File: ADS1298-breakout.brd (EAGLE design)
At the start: 33 parts, among them IC2 TPS73250DBVT, IC3 TPS73233DBVT

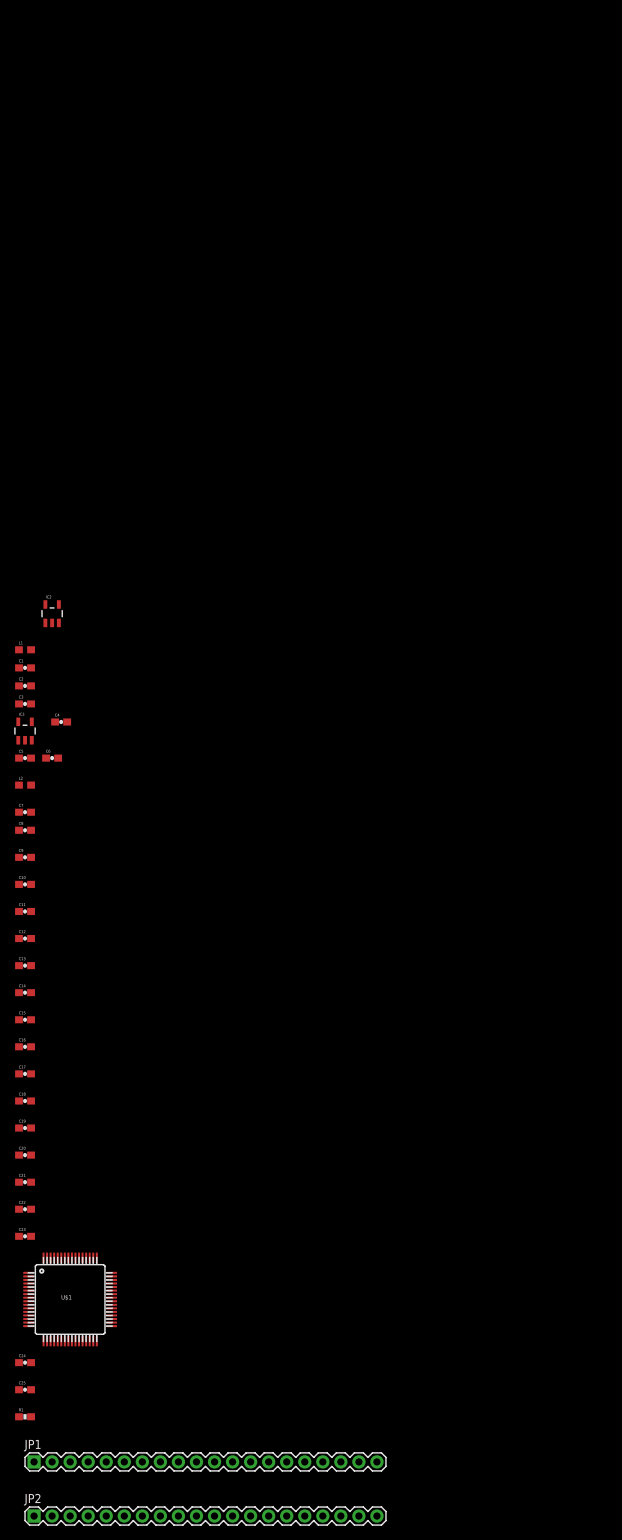
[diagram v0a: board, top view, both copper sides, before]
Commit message: schematic passes ERC
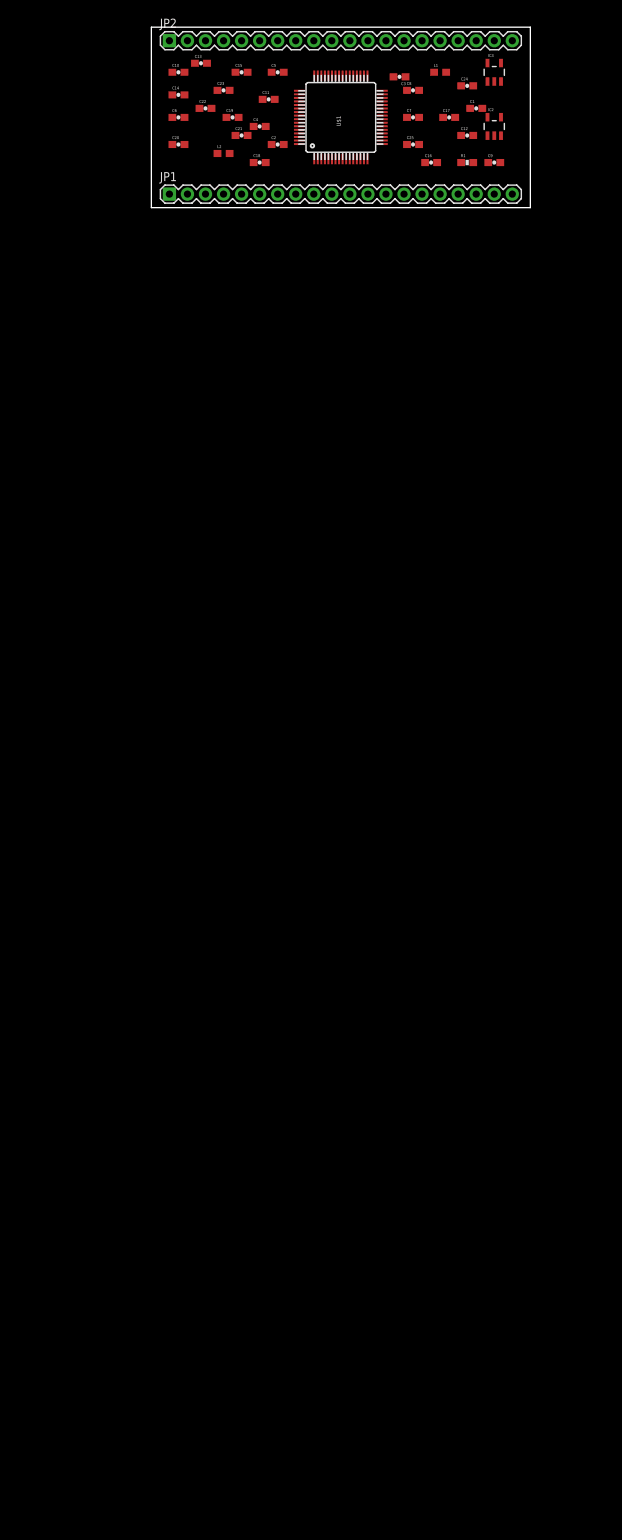
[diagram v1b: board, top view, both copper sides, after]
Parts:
- moved JP2 208.5 mm to (2.54, 23.5)
- moved C24 190.2 mm to (44.5, 17.1)
- moved R1 187.2 mm to (44.5, 6.35)
- moved C25 183.6 mm to (36.8, 8.89)
- moved JP1 179.4 mm to (2.54, 1.91)
- moved U$1 170.7 mm to (26.7, 12.7), turned to 90 degrees
- moved C23 163.7 mm to (10.2, 16.5)
- moved C22 157.0 mm to (7.62, 14.0)
- moved C21 150.4 mm to (12.7, 10.2)
- moved C17 147.3 mm to (41.9, 12.7)
- moved C19 145.2 mm to (11.4, 12.7)
- moved C20 143.9 mm to (3.81, 8.89)
- moved C16 137.0 mm to (39.4, 6.35)
- moved C15 136.8 mm to (12.7, 19.1)
- moved C18 136.1 mm to (15.2, 6.35)
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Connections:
- removed net AVSS: C10.2, C22.2, C23.2, C7.2, C8.2, C9.2, JP2.2, U$1.20, U$1.23, U$1.25, U$1.32, U$1.53, U$1.57, U$1.58
- removed net DVDD_1: U$1.48
- removed net DVDD_2: U$1.50
- removed net N$10: JP2.1
- removed net N$6: C19.1, C20.1
- new net VSS: C10.2, C15.1, C16.1, C18.2, C19.2, C20.2, C21.2, C7.2, C8.2, C9.2, JP2.2, U$1.20, U$1.23, U$1.32, U$1.53, U$1.57, U$1.58
- net /PWDN: now also U$1.35
- net /RESET: now also U$1.36
- net AGND: now also C15.2, C16.2, JP2.1, U$1.31
- net CLK: now also U$1.37
- net CLKSEL: now also U$1.52
- net DAISY_IN: now also U$1.41
- net DVDD: now also U$1.48, U$1.50
- net GND: now also C22.2, C23.2, C24.2, U$1.25; no longer C15.2, C16.2, C18.2, C19.2, C20.2, C21.2
- net GPIO1: now also U$1.42
- net GPIO2: now also U$1.44
- net GPIO3: now also U$1.45
- net GPIO4: now also U$1.46
- net IN1N: now also U$1.15
- net IN1P: now also U$1.16
- net IN2N: now also U$1.13
- net IN2P: now also U$1.14
- net IN3N: now also U$1.11
- net IN3P: now also U$1.12
- net IN4N: now also U$1.9
- net IN4P: now also U$1.10
- net IN5N: now also U$1.7
- net IN5P: now also U$1.8
- net IN6N: now also U$1.5
- net IN6P: now also U$1.6
- net IN7N: now also U$1.3
- net IN7P: now also U$1.4
- net IN8N: now also U$1.1
- net IN8P: now also U$1.2
- net N$5: now also C19.1, C20.1
- net N$7: now also U$1.64
- net PACEOUT1: now also JP2.3, U$1.17; no longer JP2.4
- net PACEOUT2: now also JP2.4, U$1.18; no longer JP2.3
- net RLD_OUT: no longer JP1.18
- net RLD_REF: now also JP1.18
- net SPI_CLK: now also U$1.40
- net SPI_DRDY: now also U$1.47
- net SPI_IN: now also U$1.34
- net SPI_OUT: now also U$1.43
- net SPI_START: now also U$1.38
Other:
- board outline added: 53.3 x 25.4 mm

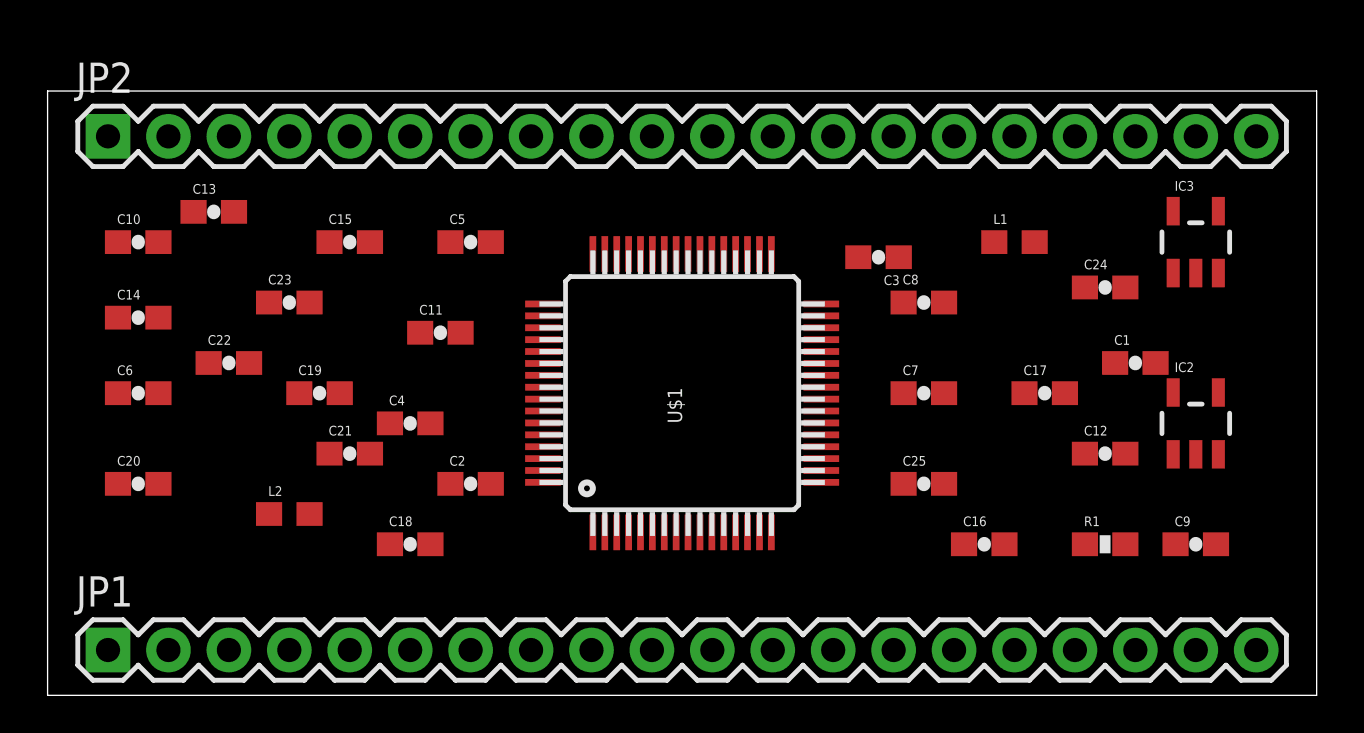
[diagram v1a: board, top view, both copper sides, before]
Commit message: changed pinout to facilate routing; board is still unrouted
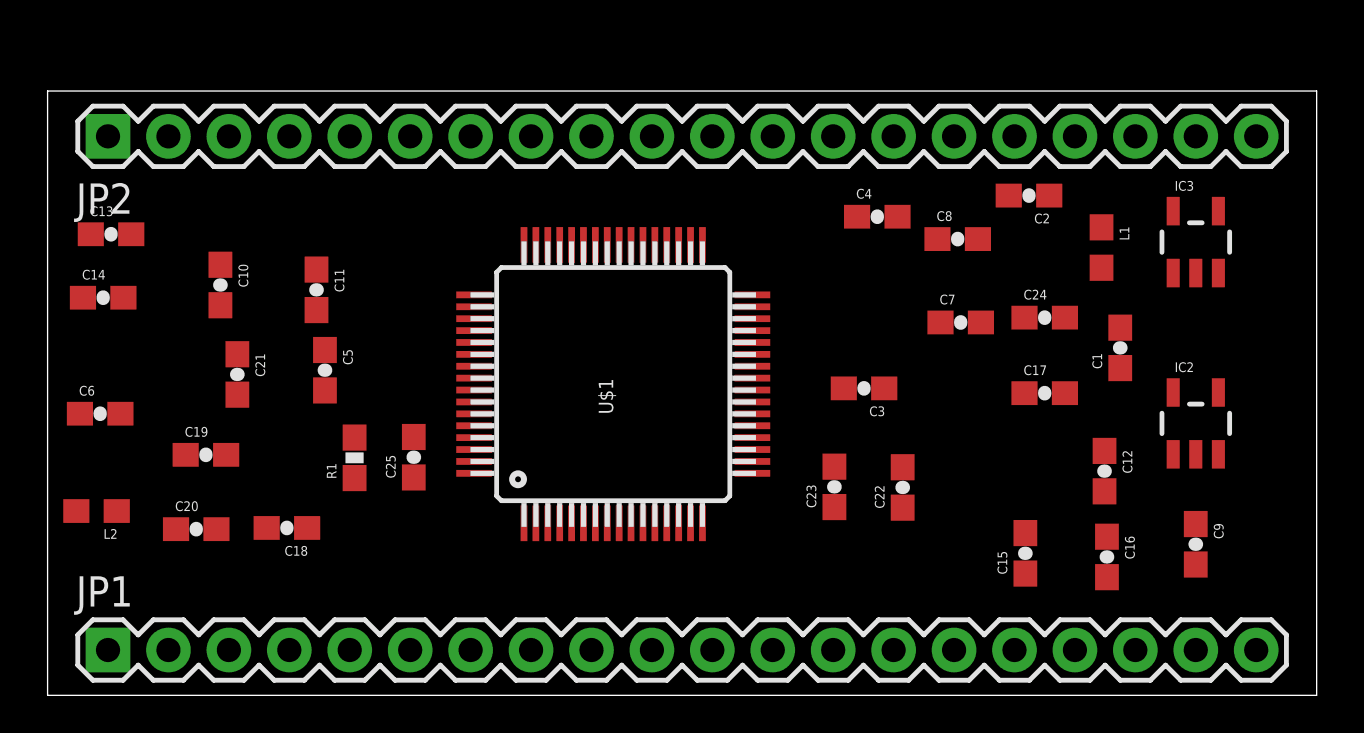
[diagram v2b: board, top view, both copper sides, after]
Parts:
- moved R1 31.8 mm to (12.9, 9.98), turned to 90 degrees
- moved C15 31.3 mm to (41.1, 5.97), turned to 90 degrees
- moved C22 28.8 mm to (35.9, 8.74), turned to 90 degrees
- moved C2 26.4 mm to (41.2, 21.0), turned to 180 degrees
- moved C23 24.2 mm to (33.1, 8.76), turned to 90 degrees
- moved C4 21.5 mm to (34.9, 20.1)
- moved C25 21.5 mm to (15.4, 10.0), turned to 90 degrees
- moved C5 8.15 mm to (11.7, 13.7), turned to 270 degrees
- moved L2 8.10 mm to (2.06, 7.75), turned to 180 degrees
- moved C21 5.78 mm to (7.98, 13.5), turned to 270 degrees
- moved C3 5.55 mm to (34.3, 12.9)
- moved C11 5.51 mm to (11.3, 17.0), turned to 270 degrees
- moved C19 5.43 mm to (6.65, 10.1)
- moved C18 5.23 mm to (10.1, 7.04), turned to 180 degrees
- moved C16 5.18 mm to (44.5, 5.82), turned to 270 degrees
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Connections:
- net /RESET renamed !RESET
- removed net /PWDN: JP2.8, U$1.35
- removed net GND: C17.2, C22.2, C23.2, C24.2, U$1.25
- removed net VSS: C10.2, C15.1, C16.1, C18.2, C19.2, C20.2, C21.2, C7.2, C8.2, C9.2, JP2.2, U$1.20, U$1.23, U$1.32, U$1.53, U$1.57, U$1.58
- new net !PWDN: JP2.6, U$1.35
- net AGND: now also C10.2, C15.1, C16.1, C17.2, C18.2, C19.2, C20.2, C21.2, C22.2, C23.2, C24.2, C7.2, C8.2, C9.2, U$1.20, U$1.23, U$1.25, U$1.32, U$1.53, U$1.57, U$1.58
- net CLK: now also JP2.8; no longer JP2.13
- net CLKSEL: now also JP2.9; no longer JP2.14
- net GPIO1: now also JP2.19; no longer JP2.12
- net GPIO2: now also JP2.18; no longer JP2.11
- net GPIO3: now also JP2.17; no longer JP2.10
- net GPIO4: now also JP2.16; no longer JP2.9
- net SPI_CLK: now also JP2.14; no longer JP2.17
- net SPI_CS: now also JP2.11; no longer JP2.18
- net SPI_DRDY: now also JP2.15; no longer JP2.19
- net SPI_IN: now also JP2.13; no longer JP2.16
- net SPI_OUT: now also JP2.12; no longer JP2.15
- net SPI_START: now also JP2.10; no longer JP2.6
- net VREFP: now also JP2.2

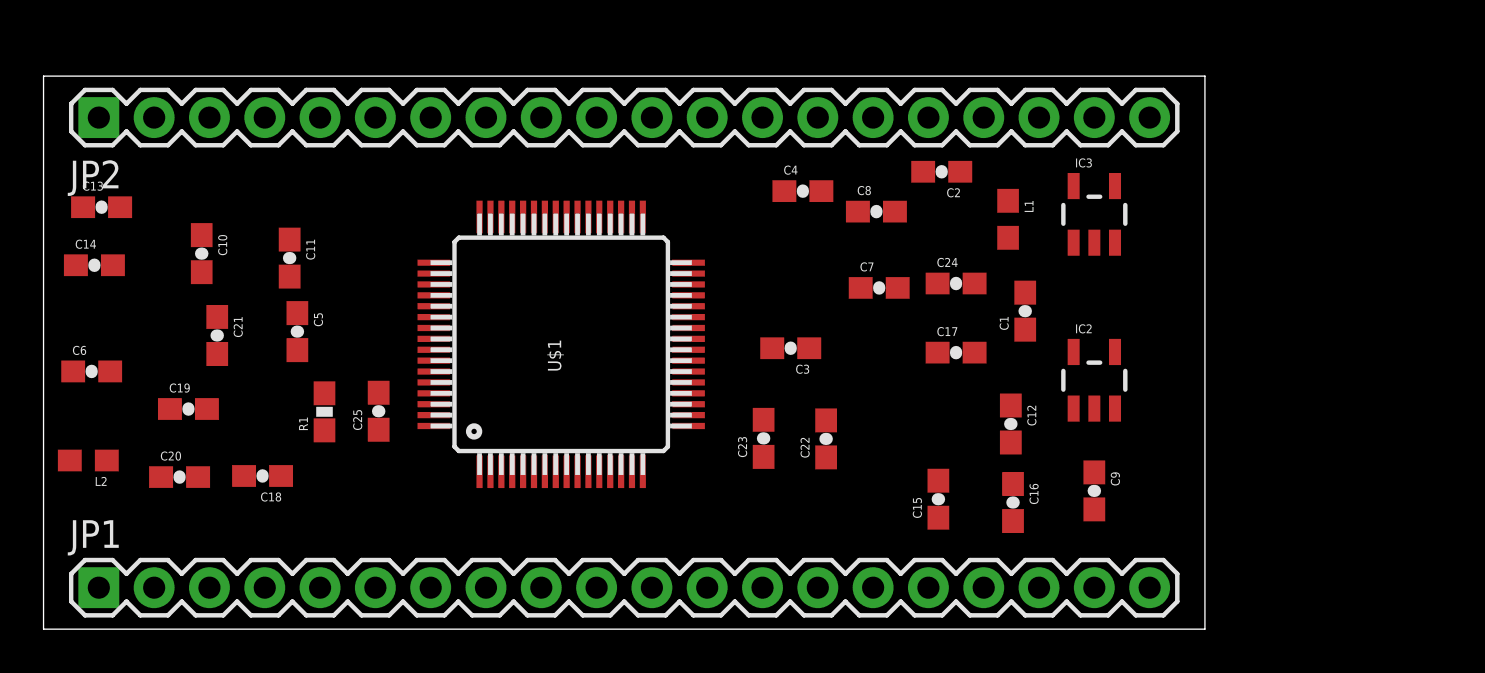
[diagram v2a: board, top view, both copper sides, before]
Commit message: corrected minor errors in schematic; changed from 20 to 24 pin headers; board partially routed
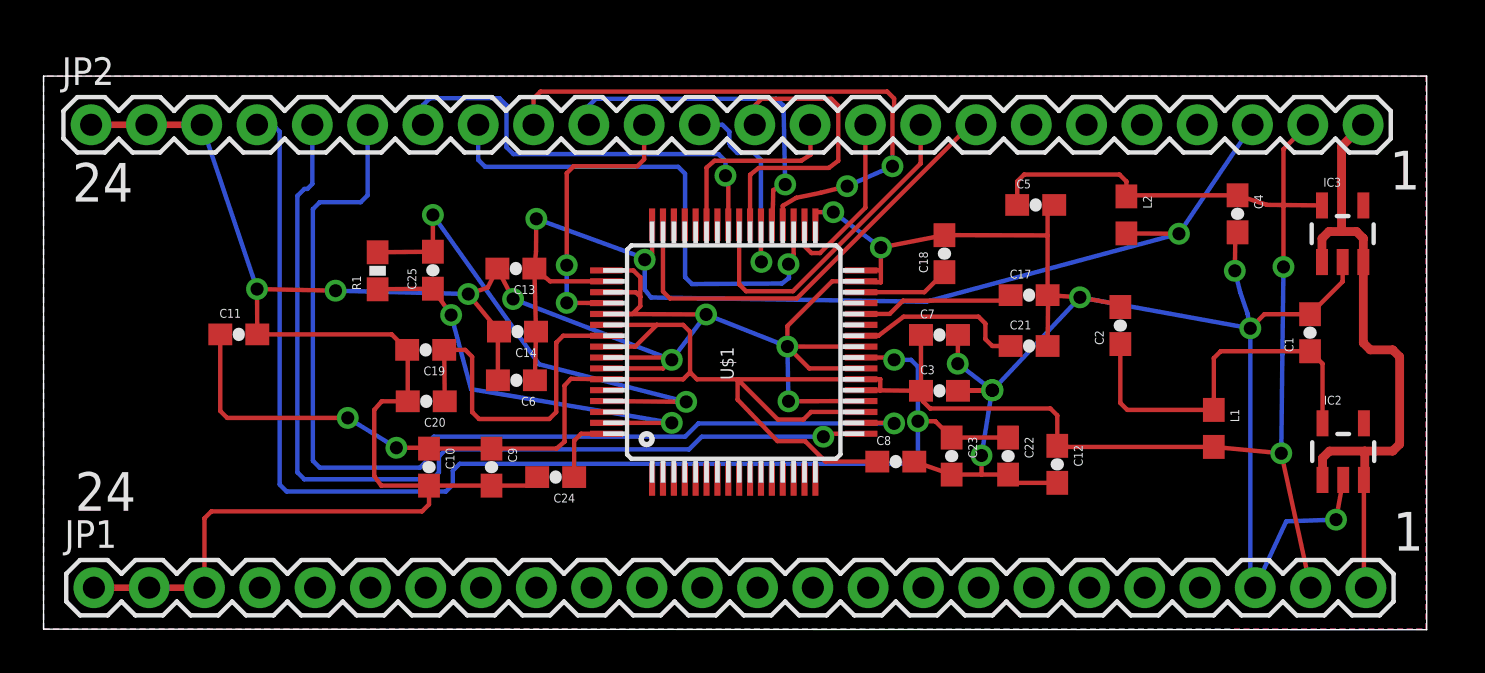
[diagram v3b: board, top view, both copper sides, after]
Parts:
- removed C15, C16: 1uF, SparkFun-Passives:0603-CAP
- JP1, JP2: value M20 -> M24; device SparkFun-Connectors:1X20 -> SparkFun-Connectors:1X24
- moved L2 49.0 mm to (49.7, 19.0), turned to 270 degrees
- moved C21 37.3 mm to (45.3, 13.0), turned to 0 degrees
- moved C5 34.4 mm to (45.6, 19.5), turned to 0 degrees
- moved C18 32.9 mm to (41.4, 17.2), turned to 90 degrees
- moved C9 27.7 mm to (20.6, 7.44)
- moved JP1 26.4 mm to (29.0, 1.91)
- moved JP2 26.3 mm to (28.9, 23.2)
- moved C24 20.4 mm to (23.5, 6.99), turned to 180 degrees
- moved C4 20.0 mm to (54.8, 19.1), turned to 270 degrees
- moved C14 19.7 mm to (21.8, 13.7), turned to 180 degrees
- moved C6 19.5 mm to (21.7, 11.4), turned to 180 degrees
- moved C13 19.2 mm to (21.7, 16.6), turned to 180 degrees
- moved C10 14.3 mm to (17.7, 7.44)
- moved L1 13.5 mm to (53.7, 9.22)
- moved C1 13.1 mm to (58.2, 13.6)
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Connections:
- net !PWDN: now also JP2.9; no longer JP2.6
- net !RESET: now also JP2.10; no longer JP2.7
- net AGND: now also JP1.2, JP1.23, JP1.3, JP1.4, JP2.2, JP2.3, JP2.4; no longer C15.1, C15.2, C16.1, C16.2, JP1.1, JP2.1
- net AVDD: now also JP1.24, JP2.24; no longer JP1.20
- net CLK: now also JP2.11; no longer JP2.8
- net CLKSEL: now also JP2.12; no longer JP2.9
- net DAISY_IN: now also JP2.8; no longer JP2.5
- net DVDD: now also JP2.23; no longer JP2.20
- net GPIO1: now also JP2.22; no longer JP2.19
- net GPIO2: now also JP2.21; no longer JP2.18
- net GPIO3: now also JP2.20; no longer JP2.17
- net GPIO4: now also JP2.19; no longer JP2.16
- net IN1N: now also JP1.19; no longer JP1.16
- net IN1P: now also JP1.20; no longer JP1.17
- net IN2N: now also JP1.17; no longer JP1.14
- net IN2P: now also JP1.18; no longer JP1.15
- net IN3N: now also JP1.15; no longer JP1.12
- net IN3P: now also JP1.16; no longer JP1.13
- net IN4N: now also JP1.13; no longer JP1.10
- net IN4P: now also JP1.14; no longer JP1.11
- net IN5N: now also JP1.11; no longer JP1.8
- net IN5P: now also JP1.12; no longer JP1.9
- net IN6N: now also JP1.9; no longer JP1.6
- net IN6P: now also JP1.10; no longer JP1.7
- net IN7N: now also JP1.7; no longer JP1.4
- net IN7P: now also JP1.8; no longer JP1.5
- net IN8N: now also JP1.5; no longer JP1.2
- net IN8P: now also JP1.6; no longer JP1.3
- net PACEOUT1: now also JP2.6; no longer JP2.3
- net PACEOUT2: now also JP2.7; no longer JP2.4
- net RLD_IN: now also JP1.22; no longer JP1.19
- net RLD_REF: now also JP1.21; no longer JP1.18
- net SPI_CLK: now also JP2.17; no longer JP2.14
- net SPI_CS: now also JP2.14; no longer JP2.11
- net SPI_DRDY: now also JP2.18; no longer JP2.15
- net SPI_IN: now also JP2.16; no longer JP2.13
- net SPI_OUT: now also JP2.15; no longer JP2.12
- net SPI_START: now also JP2.13; no longer JP2.10
- net VCC: now also JP1.25, JP2.25
- net VREFP: now also JP2.5; no longer JP2.2
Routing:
- net AGND: track 0.00 -> 211.2 mm, vias 0 -> 18
- net AVDD: track 0.00 -> 107.5 mm, vias 0 -> 4
- net VREFP: track 0.00 -> 59.5 mm, vias 0 -> 2
- net DVDD: track 0.00 -> 53.0 mm, vias 0 -> 3
- net PACEOUT2: track 0.00 -> 47.2 mm, vias 0 -> 1
- net PACEOUT1: track 0.00 -> 43.6 mm, vias 0 -> 1
- net VCC: track 0.00 -> 30.4 mm
- net !RESET: track 0.00 -> 27.4 mm, vias 0 -> 2
- net !PWDN: track 0.00 -> 23.6 mm, vias 0 -> 1
- net RLD_INV: track 0.00 -> 23.3 mm, vias 0 -> 2
- net SPI_DRDY: track 0.00 -> 20.9 mm
- net DAISY_IN: track 0.00 -> 20.2 mm, vias 0 -> 1
- net RLD_OUT: track 0.00 -> 19.9 mm, vias 0 -> 2
- net N$2: track 0.00 -> 17.6 mm
- net N$1: track 0.00 -> 16.1 mm
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- added copper zone on layer 16, net AGND
- added copper zone on layer 1, net N$6
- added copper zone on layer 16, net N$9
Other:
- board size 53.3 x 25.4 mm -> 63.5 x 25.4 mm
- board text added: "1"
- board text added: "24"
